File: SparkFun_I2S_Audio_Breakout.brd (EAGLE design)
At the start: 20.3 x 20.3 mm, 45 parts, among them IC1 MAX98375A

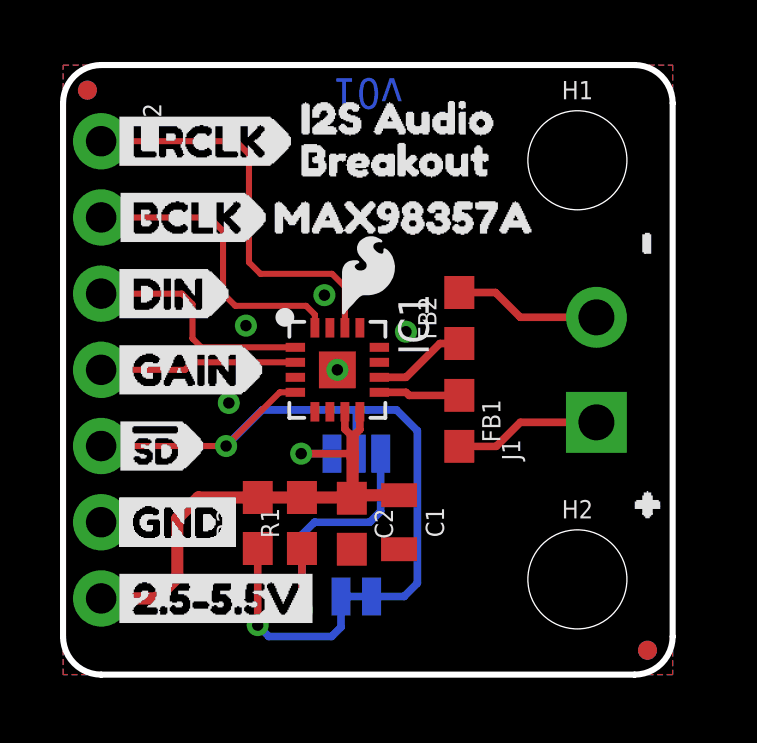
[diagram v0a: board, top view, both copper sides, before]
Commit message: Design review changes
Moved buzzard labels away from headers slightly
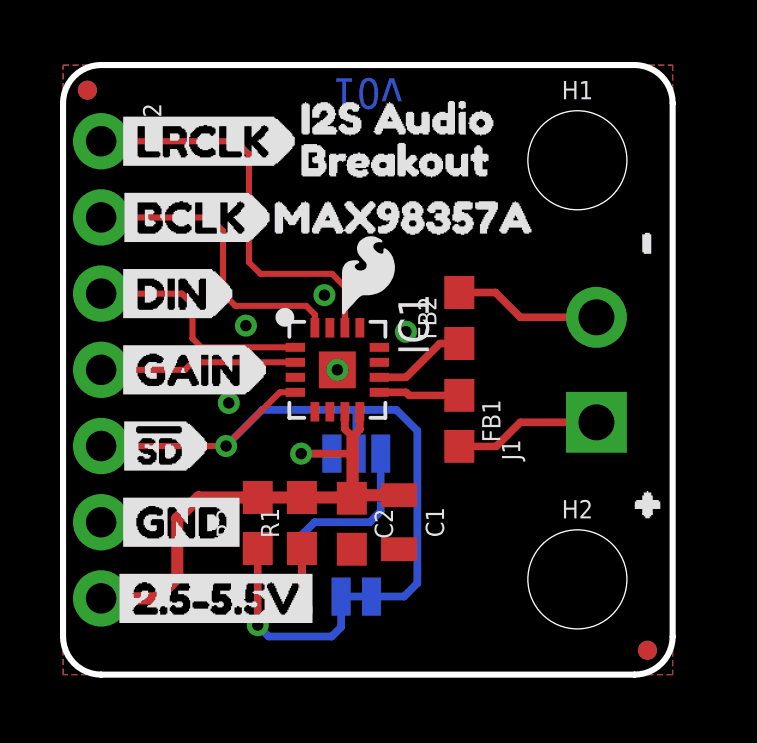
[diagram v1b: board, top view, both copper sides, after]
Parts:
- removed U$21: (no value), buzzard_labels:GND9
- moved U$11 0.13 mm to (1.52, 17.8)
- moved U$12 0.13 mm to (1.52, 15.2)
- moved U$13 0.13 mm to (1.52, 12.7)
- moved U$14 0.13 mm to (1.52, 10.2)
- moved U$2 0.13 mm to (1.52, 5.08)
- moved U$20 0.13 mm to (1.40, 7.62)
- moved U$23 0.13 mm to (1.52, 5.08)
- moved U$3 0.13 mm to (1.40, 7.62)
- moved U$4 0.13 mm to (1.52, 10.2)
- moved U$5 0.13 mm to (1.52, 12.7)
- moved U$6 0.13 mm to (1.52, 15.2)
- moved U$7 0.13 mm to (1.52, 17.8)
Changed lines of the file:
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@@
 <layer number="27" name="tValues" color="7" fill="1" visible="no" active="yes"/>
 <layer number="28" name="bValues" color="7" fill="1" visible="no" active="yes"/>
-<layer number="29" name="tStop" color="7" fill="3" visible="no" active="yes"/>
+<layer number="29" name="tStop" color="7" fill="3" visible="yes" active="yes"/>
 <layer number="30" name="bStop" color="7" fill="6" visible="no" active="yes"/>
 <layer number="31" name="tCream" color="7" fill="4" visible="no" active="yes"/>
@@
 <layer number="45" name="Holes" color="7" fill="1" visible="no" active="yes"/>
 <layer number="46" name="Milling" color="3" fill="1" visible="no" active="yes"/>
-<layer number="47" name="Measures" color="7" fill="1" visible="no" active="yes"/>
+<layer number="47" name="Measures" color="7" fill="1" visible="yes" active="yes"/>
 <layer number="48" name="Document" color="7" fill="1" visible="yes" active="yes"/>
 <layer number="49" name="Reference" color="7" fill="1" visible="yes" active="yes"/>
@@
 <element name="FD4" library="SparkFun-Aesthetics" package="FIDUCIAL-MICRO" value="FIDUCIALUFIDUCIAL" x="0.8128" y="19.4818" rot="MR0"/>
 <element name="U$1" library="buzzard_labels" package="2#5#5#5V13" value="" x="1.397" y="2.54"/>
-<element name="U$2" library="buzzard_labels" package="GND9" value="" x="1.397" y="5.08"/>
-<element name="U$3" library="buzzard_labels" package="#SD7" value="" x="1.27" y="7.62"/>
-<element name="U$4" library="buzzard_labels" package="GAIN6" value="" x="1.397" y="10.16"/>
-<element name="U$5" library="buzzard_labels" package="DIN5" value="" x="1.397" y="12.7"/>
-<element name="U$6" library="buzzard_labels" package="BCLK4" value="" x="1.397" y="15.24"/>
-<element name="U$7" library="buzzard_labels" package="LRCLK3" value="" x="1.397" y="17.78"/>
+<element name="U$2" library="buzzard_labels" package="GND9" value="" x="1.524" y="5.08"/>
+<element name="U$3" library="buzzard_labels" package="#SD7" value="" x="1.397" y="7.62"/>
+<element name="U$4" library="buzzard_labels" package="GAIN6" value="" x="1.524" y="10.16"/>
+<element name="U$5" library="buzzard_labels" package="DIN5" value="" x="1.524" y="12.7"/>
+<element name="U$6" library="buzzard_labels" package="BCLK4" value="" x="1.524" y="15.24"/>
+<element name="U$7" library="buzzard_labels" package="LRCLK3" value="" x="1.524" y="17.78"/>
 <element name="U$8" library="buzzard_labels" package="I2S_AUDIO0" value="" x="6.985" y="18.542"/>
 <element name="U$9" library="buzzard_labels" package="BREAKOUT1" value="" x="6.985" y="17.145"/>
 <element name="U$10" library="buzzard_labels" package="MAX98357A2" value="" x="6.096" y="15.24"/>
-<element name="U$11" library="buzzard_labels" package="LRCLK3" value="" x="1.397" y="17.78" rot="MR180"/>
-<element name="U$12" library="buzzard_labels" package="BCLK4" value="" x="1.397" y="15.24" rot="MR180"/>
-<element name="U$13" library="buzzard_labels" package="DIN5" value="" x="1.397" y="12.7" rot="MR180"/>
-<element name="U$14" library="buzzard_labels" package="GAIN6" value="" x="1.397" y="10.16" rot="MR180"/>
-<element name="U$20" library="buzzard_labels" package="#SD7" value="" x="1.27" y="7.62" rot="MR180"/>
-<element name="U$21" library="buzzard_labels" package="GND9" value="" x="1.397" y="5.08"/>
+<element name="U$11" library="buzzard_labels" package="LRCLK3" value="" x="1.524" y="17.78" rot="MR180"/>
+<element name="U$12" library="buzzard_labels" package="BCLK4" value="" x="1.524" y="15.24" rot="MR180"/>
+<element name="U$13" library="buzzard_labels" package="DIN5" value="" x="1.524" y="12.7" rot="MR180"/>
+<element name="U$14" library="buzzard_labels" package="GAIN6" value="" x="1.524" y="10.16" rot="MR180"/>
+<element name="U$20" library="buzzard_labels" package="#SD7" value="" x="1.397" y="7.62" rot="MR180"/>
 <element name="U$22" library="buzzard_labels" package="VDD8" value="" x="1.397" y="2.54" rot="MR180"/>
 <element name="U$16" library="buzzard_labels" package="MONO12" value="" x="7.112" y="1.016" rot="MR180"/>
@@
 <element name="U$17" library="buzzard_labels" package="L10" value="" x="9.525" y="8.89" rot="MR180"/>
 <element name="U$18" library="buzzard_labels" package="R11" value="" x="7.874" y="8.89" rot="MR180"/>
-<element name="U$23" library="buzzard_labels" package="GND9" value="" x="1.397" y="5.08" rot="MR180"/>
+<element name="U$23" library="buzzard_labels" package="GND9" value="" x="1.524" y="5.08" rot="MR180"/>
 <element name="U$24" library="buzzard_labels" package="#14" value="" x="17.907" y="5.842"/>
 <element name="U$25" library="buzzard_labels" package="#15" value="" x="19.177" y="12.827" rot="R90"/>

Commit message: Updated Bottom Silk
Used new buzzard labels so the bottom of the board is more readable within Eagle.
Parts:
- removed U$24: (no value), buzzard_labels:#14
- removed U$25: (no value), buzzard_labels:#15
- U$11: device buzzard_labels:LRCLK3 -> buzzard_labels (8):LRCLK0
- U$12: device buzzard_labels:BCLK4 -> buzzard_labels (8):BCLK1
- U$13: device buzzard_labels:DIN5 -> buzzard_labels (8):DIN2
- U$14: device buzzard_labels:GAIN6 -> buzzard_labels (8):GAIN3
- U$20: device buzzard_labels:#SD7 -> buzzard_labels (8):#SD4
- moved U$11 6.22 mm to (7.75, 17.8), turned to 0 degrees
- moved U$19 5.72 mm to (12.6, 5.84), turned to 0 degrees
- moved U$12 5.46 mm to (6.99, 15.2), turned to 0 degrees
- moved U$14 5.33 mm to (6.86, 10.2), turned to 0 degrees
- moved U$16 5.21 mm to (12.3, 1.14), turned to 0 degrees
- moved U$22 4.95 mm to (6.35, 2.54), turned to 0 degrees
- moved U$23 4.83 mm to (6.35, 5.08), turned to 0 degrees
- moved U$13 4.19 mm to (5.71, 12.7), turned to 0 degrees
- moved U$20 3.68 mm to (5.08, 7.62), turned to 0 degrees
- moved U$18 2.16 mm to (10.0, 8.89), turned to 0 degrees
- moved U$17 2.16 mm to (11.7, 8.89), turned to 0 degrees
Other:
- board text added: "+"
- board text added: "-"
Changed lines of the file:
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@@
 <layer number="45" name="Holes" color="7" fill="1" visible="no" active="yes"/>
 <layer number="46" name="Milling" color="3" fill="1" visible="no" active="yes"/>
-<layer number="47" name="Measures" color="7" fill="1" visible="yes" active="yes"/>
+<layer number="47" name="Measures" color="7" fill="1" visible="no" active="yes"/>
 <layer number="48" name="Document" color="7" fill="1" visible="yes" active="yes"/>
 <layer number="49" name="Reference" color="7" fill="1" visible="yes" active="yes"/>
@@
 <wire x1="9.865359375" y1="10.287" x2="9.865359375" y2="10.033" width="0.2032" layer="41"/>
 <wire x1="9.017" y1="9.44118125" x2="9.271" y2="9.44118125" width="0.2032" layer="41"/>
-<text x="10.16" y="19.8755" size="1.016" layer="16" font="vector" ratio="20" rot="SR180" align="bottom-center">v01</text>
+<text x="13.97" y="0.3175" size="1.016" layer="16" font="vector" ratio="20" rot="SR0" align="bottom-center">v01</text>
 <text x="12.7635" y="-18.288" size="2.1844" layer="51" font="vector" ratio="15" align="center-left">Alex Wende</text>
 <dimension x1="0" y1="1.27" x2="20.32" y2="1.27" x3="10.16" y3="-5.08" textsize="1.27" textratio="15" layer="47" unit="inch"/>
@@
 <text x="5.08" y="-6.35" size="1.27" layer="47" font="vector" ratio="15" align="center-left">Units: Inches</text>
 <dimension x1="1.27" y1="2.54" x2="1.27" y2="0" x3="-2.54" y3="1.27" textsize="1.27" textratio="15" layer="47" unit="inch" precision="3"/>
+<text x="8.89" y="16.51" size="1.778" layer="1" font="vector" ratio="16">+</text>
+<text x="18.415" y="4.826" size="1.778" layer="21" font="vector" ratio="15">+</text>
+<text x="19.812" y="13.843" size="1.778" layer="21" font="vector" ratio="15" rot="R90">-</text>
 </plain>
 <attributes>
@@
 <element name="U$9" library="buzzard_labels" package="BREAKOUT1" value="" x="6.985" y="17.145"/>
 <element name="U$10" library="buzzard_labels" package="MAX98357A2" value="" x="6.096" y="15.24"/>
-<element name="U$11" library="buzzard_labels" package="LRCLK3" value="" x="1.524" y="17.78" rot="MR180"/>
-<element name="U$12" library="buzzard_labels" package="BCLK4" value="" x="1.524" y="15.24" rot="MR180"/>
-<element name="U$13" library="buzzard_labels" package="DIN5" value="" x="1.524" y="12.7" rot="MR180"/>
-<element name="U$14" library="buzzard_labels" package="GAIN6" value="" x="1.524" y="10.16" rot="MR180"/>
-<element name="U$20" library="buzzard_labels" package="#SD7" value="" x="1.397" y="7.62" rot="MR180"/>
-<element name="U$22" library="buzzard_labels" package="VDD8" value="" x="1.397" y="2.54" rot="MR180"/>
-<element name="U$16" library="buzzard_labels" package="MONO12" value="" x="7.112" y="1.016" rot="MR180"/>
-<element name="U$19" library="buzzard_labels" package="STEREO14" value="" x="6.858" y="5.715" rot="MR180"/>
-<element name="U$17" library="buzzard_labels" package="L10" value="" x="9.525" y="8.89" rot="MR180"/>
-<element name="U$18" library="buzzard_labels" package="R11" value="" x="7.874" y="8.89" rot="MR180"/>
-<element name="U$23" library="buzzard_labels" package="GND9" value="" x="1.524" y="5.08" rot="MR180"/>
-<element name="U$24" library="buzzard_labels" package="#14" value="" x="17.907" y="5.842"/>
-<element name="U$25" library="buzzard_labels" package="#15" value="" x="19.177" y="12.827" rot="R90"/>
+<element name="U$22" library="buzzard_labels" package="VDD8" value="" x="6.35" y="2.54" rot="MR0"/>
+<element name="U$16" library="buzzard_labels" package="MONO12" value="" x="12.319" y="1.143" rot="MR0"/>
+<element name="U$19" library="buzzard_labels" package="STEREO14" value="" x="12.573" y="5.842" rot="MR0"/>
+<element name="U$17" library="buzzard_labels" package="L10" value="" x="11.684" y="8.89" rot="MR0"/>
+<element name="U$18" library="buzzard_labels" package="R11" value="" x="10.033" y="8.89" rot="MR0"/>
+<element name="U$23" library="buzzard_labels" package="GND9" value="" x="6.35" y="5.08" rot="MR0"/>
+<element name="U$11" library="buzzard_labels (8)" package="LRCLK0" value="" x="7.747" y="17.78" rot="MR0"/>
+<element name="U$12" library="buzzard_labels (8)" package="BCLK1" value="" x="6.985" y="15.24" rot="MR0"/>
+<element name="U$13" library="buzzard_labels (8)" package="DIN2" value="" x="5.715" y="12.7" rot="MR0"/>
+<element name="U$14" library="buzzard_labels (8)" package="GAIN3" value="" x="6.858" y="10.16" rot="MR0"/>
+<element name="U$20" library="buzzard_labels (8)" package="#SD4" value="" x="5.08" y="7.62" rot="MR0"/>
 </elements>
 <signals>
